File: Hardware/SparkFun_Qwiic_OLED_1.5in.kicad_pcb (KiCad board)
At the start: 2 copper layers, 34.3 x 49.5 mm, 72 parts, among them J1 Qwiic_RA, J2 Qwiic_RA, J4 Conn_01x24_FPC, J5 Conn_01x07, U2 WEO128128ASAP3N00000, U5 AP3012

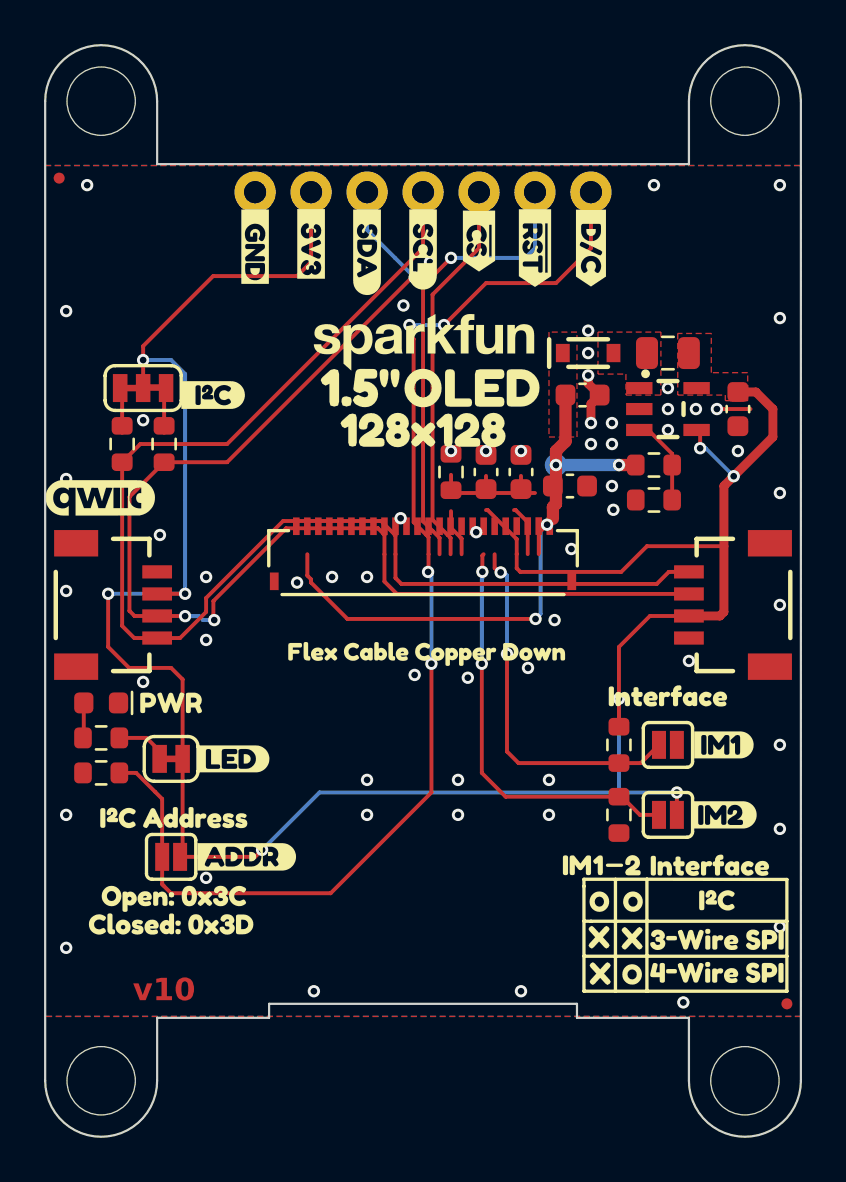
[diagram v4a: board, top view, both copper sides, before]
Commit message: Updates the OLED footprint so that the screen to fold distance is more correctly represented
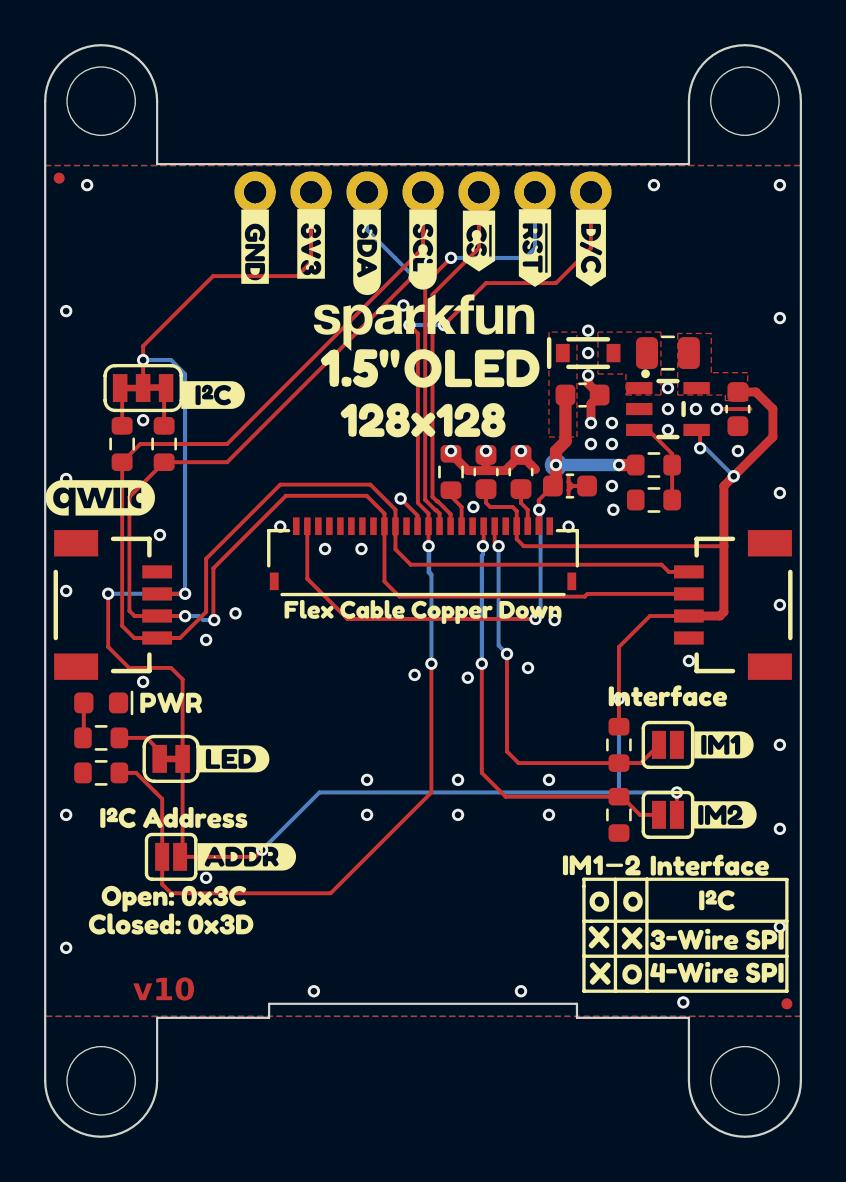
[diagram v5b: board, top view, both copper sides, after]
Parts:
- moved kibuzzard-684C656A 1.91 mm to (140.4, 87.0)
- moved G*** 0.89 mm to (140.4, 73.7)
- moved kibuzzard-68518672 0.89 mm to (142.6, 75.9)
- moved kibuzzard-6851867B 0.89 mm to (137.6, 75.9)
- moved kibuzzard-680FC73E 0.44 mm to (140.4, 78.3)
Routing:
- net GND: track 10.1 -> 13.2 mm
- net SDA/SDI: track 57.4 -> 59.8 mm
- net SCL/SCK: track 58.7 -> 60.2 mm
- net ~{RST}: track 20.8 -> 19.5 mm
- net ~{CS}: track 17.6 -> 16.4 mm
- net Net-(J4-Pin_18): track 18.9 -> 20.1 mm
- net Net-(J4-Pin_19): track 16.8 -> 17.9 mm
- net D/C: track 54.7 -> 55.8 mm
- net 12V: track 28.4 -> 29.4 mm

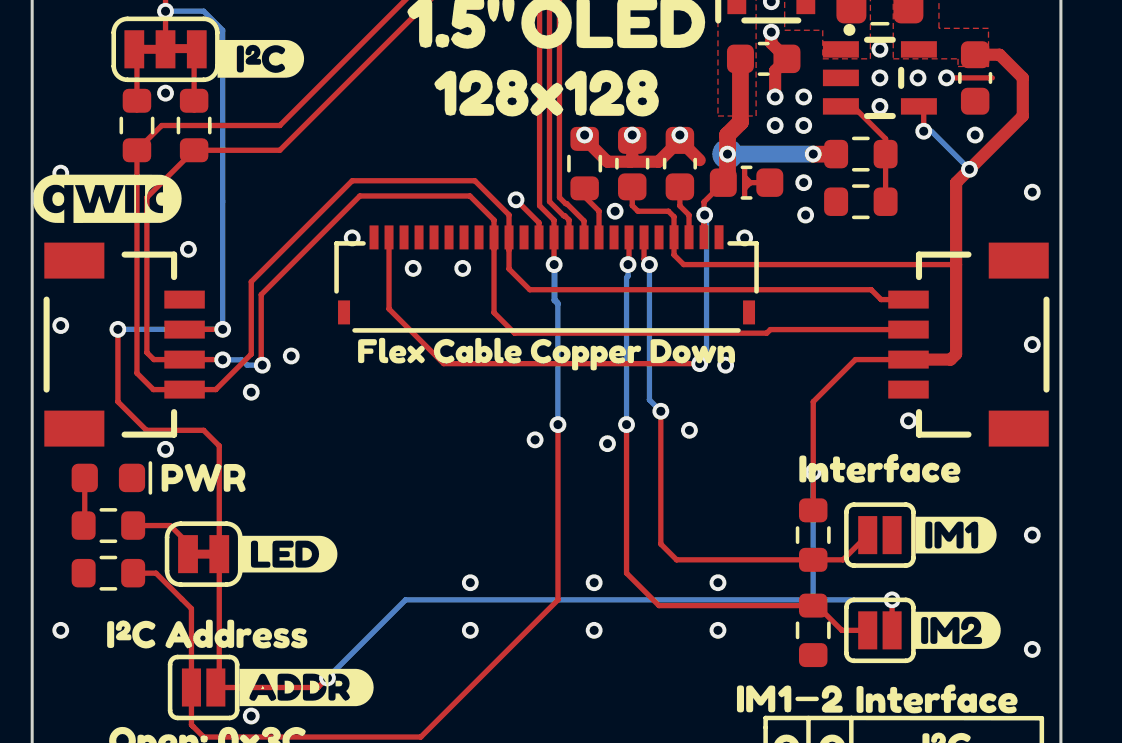
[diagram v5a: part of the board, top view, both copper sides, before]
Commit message: Moves some small traces around
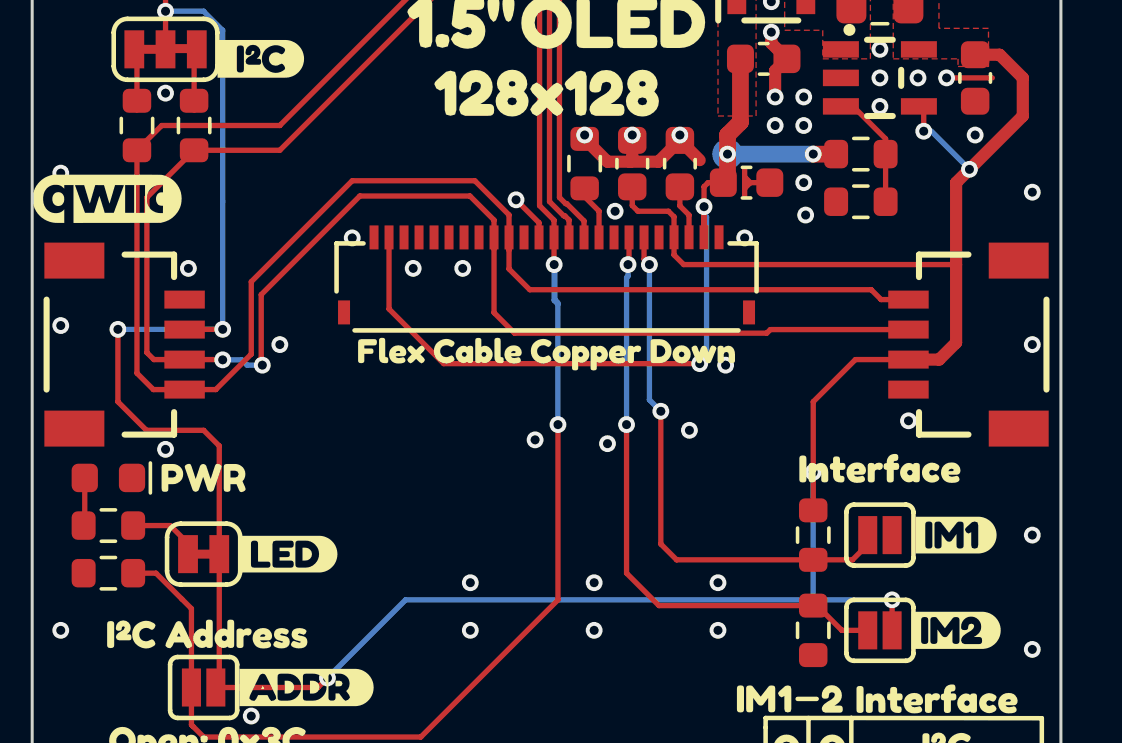
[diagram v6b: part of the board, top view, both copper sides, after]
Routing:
- net 12V: track 29.4 -> 30.4 mm
- net GND: vias 60 -> 59
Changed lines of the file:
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@@
+	)
+	(segment
+		(start 152.476 87.176)
+		(end 153.5 87.176)
+		(width 0.4064)
+		(layer "F.Cu")
+		(net 1)
 	)
 	(segment
@@
 	)
 	(segment
+		(start 154.0635 86.6125)
+		(end 154.0635 84.009)
+		(width 0.4064)
+		(layer "F.Cu")
+		(net 1)
+	)
+	(segment
 		(start 126.1235 88.581)
 		(end 127.076 89.5335)
@@
 		(end 129.5017 93.661)
 		(width 0.1778)
-		(layer "F.Cu")
-		(net 1)
-	)
-	(segment
-		(start 152.476 87.176)
-		(end 153.881 87.176)
-		(width 0.4064)
-		(layer "F.Cu")
-		(net 1)
-	)
-	(segment
-		(start 154.0635 86.9935)
-		(end 154.0635 84.009)
-		(width 0.4064)
 		(layer "F.Cu")
 		(net 1)
@@
 	)
 	(segment
-		(start 153.881 87.176)
-		(end 154.0635 86.9935)
-		(width 0.4064)
-		(layer "F.Cu")
-		(net 1)
-	)
-	(segment
 		(start 144.6609 83.0985)
 		(end 144.6609 82.4169)
@@
 	)
 	(segment
+		(start 153.5 87.176)
+		(end 154.0635 86.6125)
+		(width 0.4064)
+		(layer "F.Cu")
+		(net 1)
+	)
+	(segment
 		(start 129.616 98.106)
 		(end 132.791 98.106)
@@
 	)
 	(via
-		(at 130.5685 88.2635)
+		(at 131.521 86.676)
 		(size 0.56)
 		(drill 0.3)
@@
 	)
 	(via
-		(at 128.473 83.501)
+		(at 128.473 84.136)
 		(size 0.56)
 		(drill 0.3)
@@
 	(via
 		(at 133.934 83.12)
-		(size 0.56)
-		(drill 0.3)
-		(layers "F.Cu" "B.Cu")
-		(free yes)
-		(net 2)
-	)
-	(via
-		(at 131.902 87.057)
 		(size 0.56)
 		(drill 0.3)
@@
 		(layer "B.Cu")
 		(net 15)
-	)
-	(segment
-		(start 145.6609 82.3793)
-		(end 145.6822 82.358)
-		(width 0.1778)
-		(layer "F.Cu")
-		(net 16)
 	)
 	(segment
@@
 	)
 	(segment
-		(start 145.6609 81.9211)
-		(end 146.3035 81.2785)
+		(start 145.6609 82.0786)
+		(end 145.6609 83.0985)
 		(width 0.1778)
 		(layer "F.Cu")
@@
 	)
 	(segment
+		(start 145.6609 82.0786)
+		(end 145.6609 81.4134)
+		(width 0.1778)
+		(layer "F.Cu")
+		(net 16)
+	)
+	(segment
 		(start 149.3035 80.3285)
 		(end 149.301 80.326)
@@
 	)
 	(segment
+		(start 145.6609 81.4134)
+		(end 145.7958 81.2785)
+		(width 0.1778)
+		(layer "F.Cu")
+		(net 16)
+	)
+	(segment
 		(start 146.4435 80.326)
 		(end 146.4435 81.1385)
@@
 	)
 	(segment
+		(start 145.7958 81.2785)
+		(end 146.3035 81.2785)
+		(width 0.1778)
+		(layer "F.Cu")
+		(net 16)
+	)
+	(segment
 		(start 146.4435 79.691)
 		(end 146.875 79.2595)
@@
 	)
 	(segment
-		(start 145.6609 83.0985)
-		(end 145.6609 82.3793)
-		(width 0.1778)
-		(layer "F.Cu")
-		(net 16)
-	)
-	(segment
 		(start 136.982 87.311)
 		(end 145.5164 87.311)
@@
 	)
 	(via
-		(at 145.6822 82.358)
+		(at 145.6609 82.0786)
 		(size 0.56)
 		(drill 0.3)
@@
 	)
 	(segment
+		(start 145.6609 82.3367)
+		(end 145.745 82.4208)
+		(width 0.1778)
+		(layer "B.Cu")
+		(net 16)
+	)
+	(segment
+		(start 145.745 87.0824)
+		(end 145.5164 87.311)
+		(width 0.1778)
+		(layer "B.Cu")
+		(net 16)
+	)
+	(segment
 		(start 145.745 82.4208)
-		(end 145.6822 82.358)
+		(end 145.745 87.0824)
+		(width 0.1778)
+		(layer "B.Cu")
+		(net 16)
+	)
+	(segment
+		(start 145.6609 82.0786)
+		(end 145.6609 82.3367)
 		(width 0.1778)
 		(layer "B.Cu")
@@
 	)
 	(segment
-		(start 145.745 87.0824)
-		(end 145.745 82.4208)
-		(width 0.1778)
-		(layer "B.Cu")
-		(net 16)
-	)
-	(segment
-		(start 145.5164 87.311)
-		(end 145.745 87.0824)
-		(width 0.1778)
-		(layer "B.Cu")
-		(net 16)
-	)
-	(segment
 		(start 144.5385 81.596)
 		(end 144.856 81.596)
@@
 	)
 	(segment
+		(start 149.301 93.851)
+		(end 150.6096 93.851)
+		(width 0.1778)
+		(layer "F.Cu")
+		(net 20)
+	)
+	(segment
 		(start 143.6609 83.8299)
 		(end 143.84 84.009)
@@
 	)
 	(segment
+		(start 151.1171 93.3435)
+		(end 151.1171 93.026)
+		(width 0.1778)
+		(layer "F.Cu")
+		(net 20)
+	)
+	(segment
+		(start 150.6096 93.851)
+		(end 151.1171 93.3435)
+		(width 0.1778)
+		(layer "F.Cu")
+		(net 20)
+	)
+	(segment
 		(start 144.221 88.8985)
 		(end 144.221 93.324443)
@@
 	)
 	(segment
-		(start 150.2921 93.851)
-		(end 151.1171 93.026)
-		(width 0.1778)
-		(layer "F.Cu")
-		(net 20)
-	)
-	(segment
 		(start 143.6609 83.1035)
 		(end 143.6609 83.8299)
 		(width 0.1778)
 		(layer "F.Cu")
-		(net 20)
-	)
-	(segment
-		(start 149.301 93.851)
-		(end 150.2921 93.851)
-		(width 0.1778)
-		(layer "F.Cu")
